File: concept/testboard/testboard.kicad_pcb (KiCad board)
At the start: 2 copper layers, 85 x 40 mm, 31 parts, among them IC1 NCP1117DT33T5G, J1 Probe out 1, J2 I2C, J3 Probe out 0, J4 probe connector, J5 IO bank 0, J6 IO bank 1, J7 5V, U1 SN74CB3T16211DGGR, U2 PCA9535CPW,118

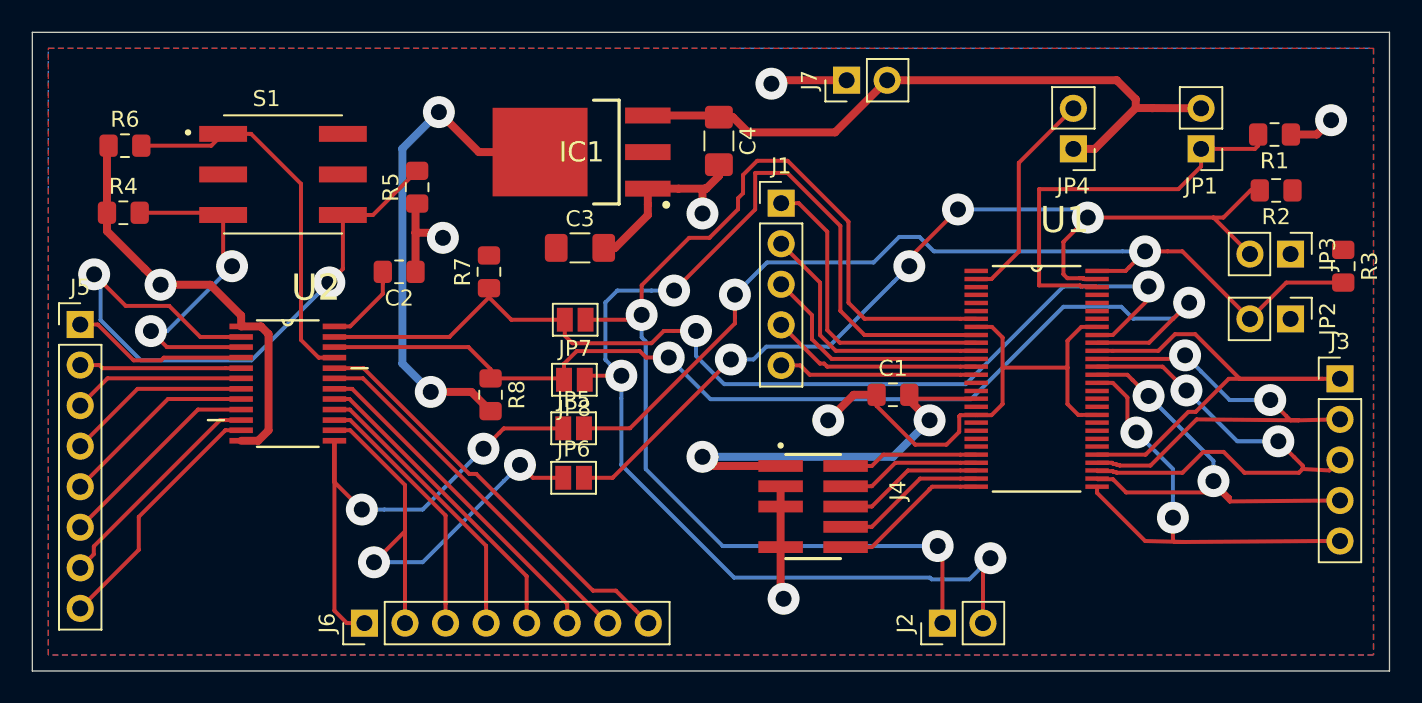
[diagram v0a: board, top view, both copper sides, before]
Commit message: Testboard layout edits to comply to manufacturer
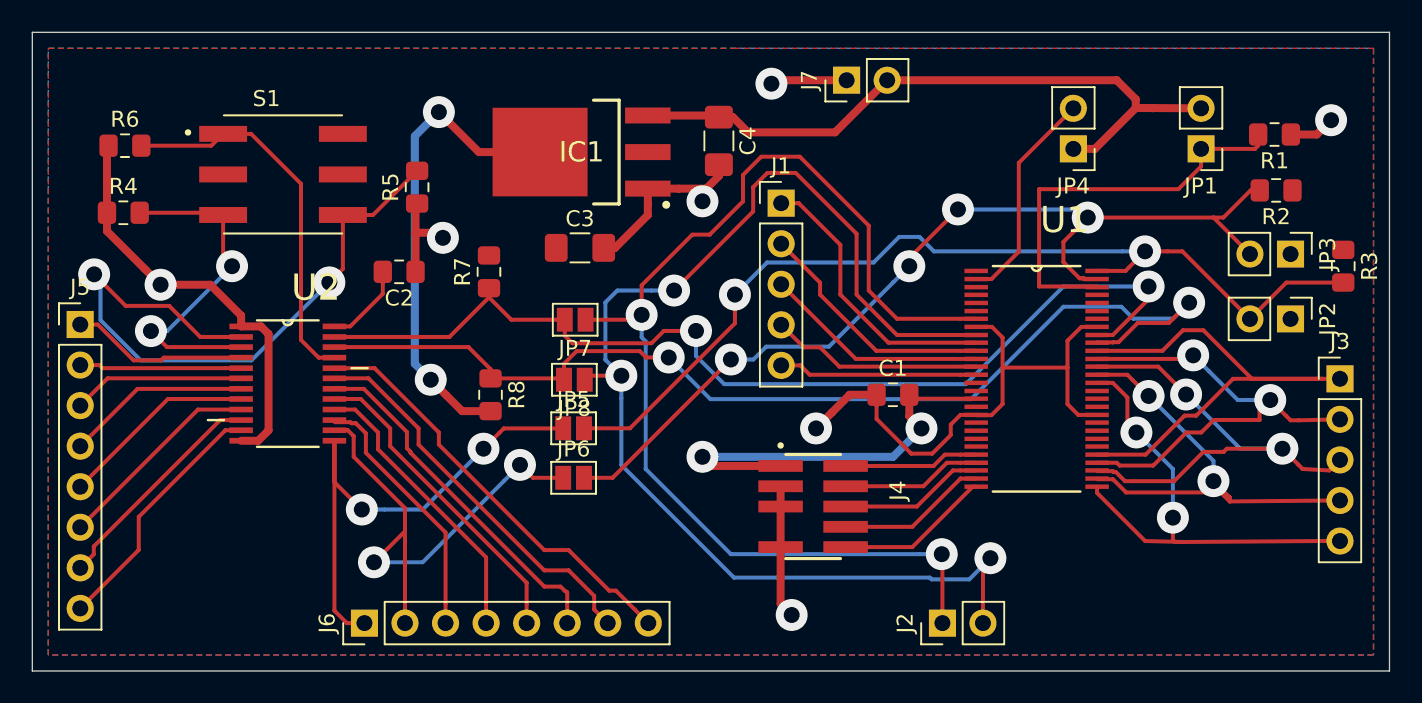
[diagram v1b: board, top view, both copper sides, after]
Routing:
- net GND: track 93.4 -> 95.6 mm
- net Net-(J1-Pad1): track 19.4 -> 17.7 mm
- net Net-(J3-Pad3): track 32.4 -> 30.9 mm
- net +3V3: track 62.8 -> 61.3 mm
- net Net-(J1-Pad2): track 16.9 -> 15.4 mm
- net /I2C_SCL_in: track 79.1 -> 77.8 mm
- net /IO1_6: track 23.5 -> 24.6 mm
- net /IO1_5: track 21.4 -> 22.4 mm
- net Net-(J3-Pad2): track 30.9 -> 30.0 mm
- net Net-(J1-Pad3): track 15.0 -> 14.2 mm
- net /I2C_SDA_in: track 72.8 -> 72.2 mm
